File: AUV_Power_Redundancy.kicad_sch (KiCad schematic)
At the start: 0 parts

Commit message: Complete first LM5050 power path
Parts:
- added J1, J2, J3: Conn_01x02, symbol Connector_Generic:Conn_01x02
- added Q1, Q2: Q_NMOS_GSD, symbol Transistor_FET:Q_NMOS_GSD
- added U1, U2: LM5050-1, Package_TO_SOT_SMD:TSOT-23-6, symbol Power_Management:LM5050-1
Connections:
- new net: J1.1 (Pin_1), Q1.2 (S), U1.4 (IN)
- new net: Q1.1 (G), U1.5 (GATE)
- new net: J3.1 (Pin_1), Q1.3 (D), U1.1 (VS), U1.6 (OUT)
- new net GND: J1.2 (Pin_2), J2.2 (Pin_2), U1.2 (GND), U1.3 (OFF), U2.2 (GND)

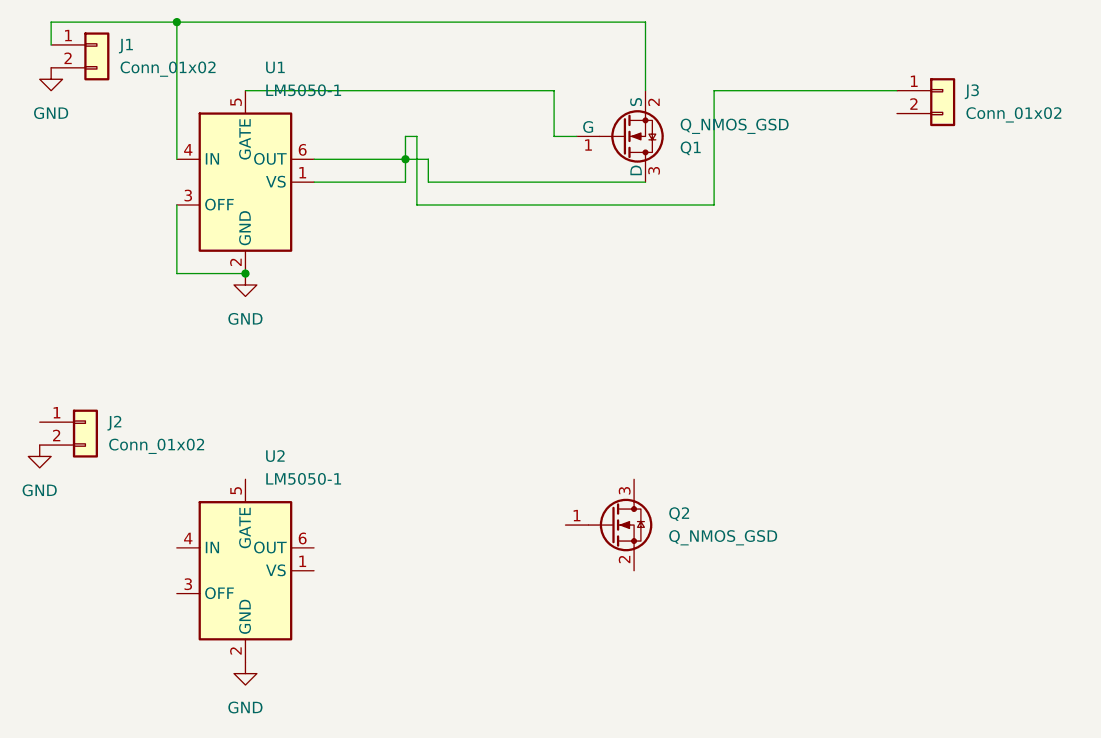
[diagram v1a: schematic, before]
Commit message: Complete dual LM5050 redundancy schematic
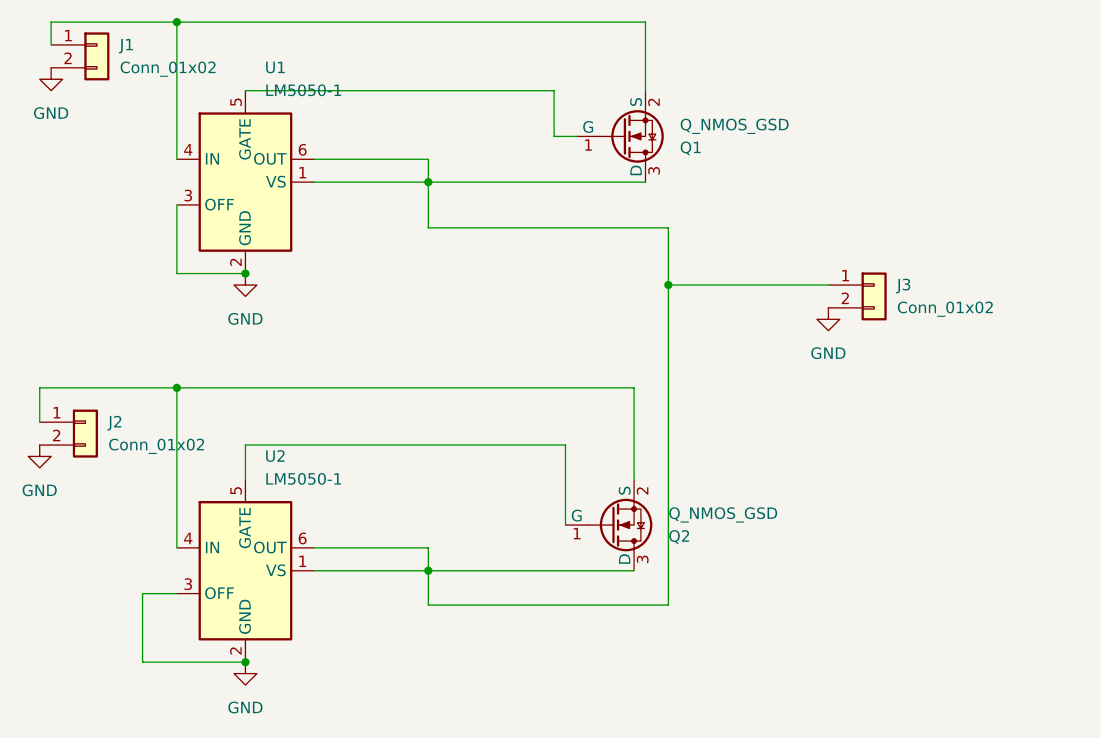
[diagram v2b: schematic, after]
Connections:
- net GND: now also J3.2 (Pin_2), U2.3 (OFF)
- net at U2.1 (VS): now also J3.1 (Pin_1), Q1.3 (D), Q2.3 (D), U1.1 (VS), U1.6 (OUT), U2.6 (OUT)
- net at U2.4 (IN): now also J2.1 (Pin_1), Q2.2 (S)
- net at U2.5 (GATE): now also Q2.1 (G)
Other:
- moved on the sheet: J3

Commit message: Assign footprints to all components
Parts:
- added C1: 0.1nF, Capacitor_SMD:C_0805_2012Metric, symbol Device:C
- added R1: 10k, Resistor_SMD:R_0805_2012Metric, symbol Device:R
- J1, J2, J3: footprint (none) -> Connector_PinHeader_2.54mm:PinHeader_1x02_P2.54mm_Vertical
- Q1, Q2: footprint (none) -> Package_TO_SOT_SMD:SOT-23
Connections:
- net GND: now also C1.2, R1.1
- net at J3.1 (Pin_1), Q1.3 (D), Q2.3 (D)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: now also C1.1, R1.2
